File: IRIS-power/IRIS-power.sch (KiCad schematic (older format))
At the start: 11 parts, among them J11 Powerpole, J12 PJ-047AH, U11 TVS1400DRV, U12 TVS1400DRV

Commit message: Updated IRIS power board for V4
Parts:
- removed U11, U12: TVS1400DRV, star-common-lib:WSON-6-1EP_2x2mm_Hand_Solder, symbol star-common-lib:TVS1400DRV
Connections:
- wire segments 63 -> 61
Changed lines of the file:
@@
 Wire Wire Line
 	1300 3750 1900 3750
-Wire Wire Line
-	1900 2900 1300 2900
 Connection ~ 1300 2900
-Wire Wire Line
-	1300 2300 1900 2300
-$Comp
-L star-common-lib:TVS1400DRV U?
-U 1 1 5F2F2145
-P 1900 2600
-AR Path="/5F38FD4F/5F2F2145" Ref="U?"  Part="1"
-AR Path="/5F2F2145" Ref="U11"  Part="1"
-F 0 "U11" H 2029 2646 50  0000 L CNN
-F 1 "TVS1400DRV" H 2029 2555 50  0000 L CNN
-F 2 "star-common-lib:WSON-6-1EP_2x2mm_Hand_Solder" H 2100 2250 50  0001 C CNN
-F 3 "http://www.ti.com/lit/ds/symlink/tvs1400.pdf" H 1800 2600 50  0001 C CNN
-	1    1900 2600
-	1    0    0    -1
-$EndComp
-Connection ~ 1900 2300
-$Comp
-L star-common-lib:TVS1400DRV U?
-U 1 1 5F2F214D
-P 1900 4050
-AR Path="/5F38FD4F/5F2F214D" Ref="U?"  Part="1"
-AR Path="/5F2F214D" Ref="U12"  Part="1"
-F 0 "U12" H 2029 4096 50  0000 L CNN
-F 1 "TVS1400DRV" H 2029 4005 50  0000 L CNN
-F 2 "star-common-lib:WSON-6-1EP_2x2mm_Hand_Solder" H 2100 3700 50  0001 C CNN
-F 3 "http://www.ti.com/lit/ds/symlink/tvs1400.pdf" H 1800 4050 50  0001 C CNN
-	1    1900 4050
-	1    0    0    -1
-$EndComp
 Connection ~ 1900 3750
 Wire Wire Line
@@
 Wire Wire Line
 	1300 4350 1900 4350
-Connection ~ 1900 4350
 Wire Wire Line
 	1900 3750 3100 3750
-Wire Wire Line
-	1900 2300 2800 2300
 Wire Wire Line
 	2800 2300 2800 3550
 Connection ~ 2800 2300
 Wire Wire Line
-	1900 2900 2600 2900
-Wire Wire Line
 	2600 2900 2600 2500
 Wire Wire Line
 	2600 2500 7850 2500
-Connection ~ 1900 2900
 Wire Wire Line
 	9500 4650 9500 2400
@@
 	1    0    0    -1
 $EndComp
+Wire Wire Line
+	1300 2900 2600 2900
+Wire Wire Line
+	1300 2300 2800 2300
 $EndSCHEMATC

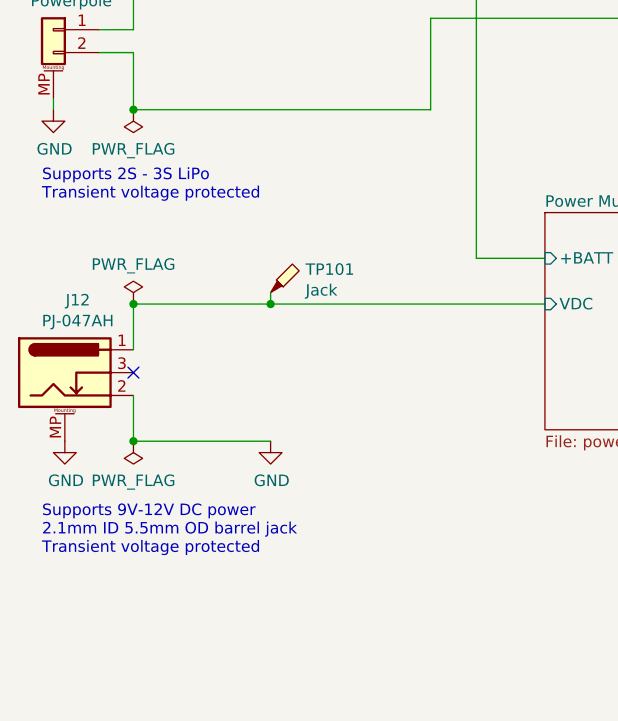
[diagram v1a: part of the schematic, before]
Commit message: Improved fuel gauge layout
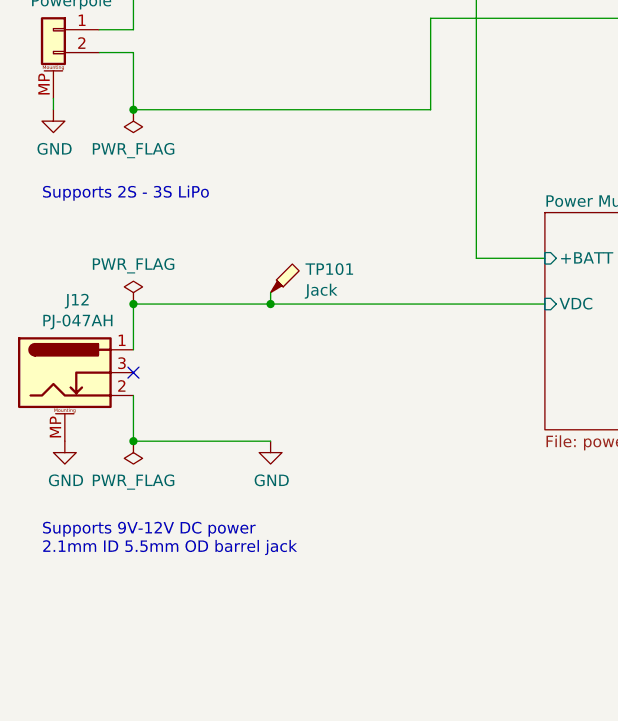
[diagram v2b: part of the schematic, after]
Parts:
- J11: Digikey PN (none) -> 2243-1336G1-ND
- J12: Digikey PN (none) -> CP-047AH-ND
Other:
- note added: "Supports 2S - 3S LiPo"
- note added: "Supports 9V-12V DC power\n2.1mm ID 5.5mm OD barrel jack"
- note removed: "Supports 2S - 3S LiPo\nTransient voltage protected"
- note removed: "Supports 9V-12V DC power\n2.1mm ID 5.5mm OD barrel jack\nTransient voltage protected"
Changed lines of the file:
@@
 	1300 2650 1300 2900
 Text Notes 900  3300 0    50   ~ 0
-Supports 2S - 3S LiPo\nTransient voltage protected
+Supports 2S - 3S LiPo
 $Comp
 L power:GND #PWR0101
@@
 F 2 "star-common-lib:CUI_PJ-047AH" H 1050 4010 50  0001 C CNN
 F 3 "~" H 1050 4010 50  0001 C CNN
+F 4 "CP-047AH-ND" H 1000 4050 50  0001 C CNN "Digikey PN"
 	1    1000 4050
 	1    0    0    -1
@@
 Wire Wire Line
 	1300 3950 1300 3750
-Text Notes 900  4850 0    50   ~ 0
-Supports 9V-12V DC power\n2.1mm ID 5.5mm OD barrel jack\nTransient voltage protected
 $Comp
 L power:PWR_FLAG #FLG?
@@
 F 2 "star-common-lib:Powerpole_1336G1" H 950 2550 50  0001 C CNN
 F 3 "~" H 950 2550 50  0001 C CNN
+F 4 "2243-1336G1-ND" H 950 2550 50  0001 C CNN "Digikey PN"
 	1    950  2550
 	-1   0    0    -1
@@
 Wire Wire Line
 	1300 2300 2800 2300
+Text Notes 900  4850 0    50   ~ 0
+Supports 9V-12V DC power\n2.1mm ID 5.5mm OD barrel jack
 $EndSCHEMATC

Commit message: Adjusted silkscreen
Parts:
- TP101, TP102, TP103, TP104, TP105, TP106, TP107: Digikey PN (none) -> 36-5006-ND
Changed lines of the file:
@@
 F 2 "TestPoint:TestPoint_Keystone_5000-5004_Miniature" H 4550 3500 50  0001 C CNN
 F 3 "~" H 4550 3500 50  0001 C CNN
+F 4 "36-5006-ND" H 4350 3500 50  0001 C CNN "Digikey PN"
 	1    4350 3500
 	1    0    0    -1
@@
 F 2 "TestPoint:TestPoint_Keystone_5000-5004_Miniature" H 4600 2250 50  0001 C CNN
 F 3 "~" H 4600 2250 50  0001 C CNN
+F 4 "36-5006-ND" H 4400 2250 50  0001 C CNN "Digikey PN"
 	1    4400 2250
 	1    0    0    -1
@@
 F 2 "TestPoint:TestPoint_Keystone_5000-5004_Miniature" H 6100 3500 50  0001 C CNN
 F 3 "~" H 6100 3500 50  0001 C CNN
+F 4 "36-5006-ND" H 5900 3500 50  0001 C CNN "Digikey PN"
 	1    5900 3500
 	1    0    0    -1
@@
 F 2 "TestPoint:TestPoint_Keystone_5000-5004_Miniature" H 7500 5000 50  0001 C CNN
 F 3 "~" H 7500 5000 50  0001 C CNN
+F 4 "36-5006-ND" H 7300 5000 50  0001 C CNN "Digikey PN"
 	1    7300 5000
 	1    0    0    -1
@@
 F 2 "TestPoint:TestPoint_Keystone_5000-5004_Miniature" H 7700 3550 50  0001 C CNN
 F 3 "~" H 7700 3550 50  0001 C CNN
+F 4 "36-5006-ND" H 7500 3550 50  0001 C CNN "Digikey PN"
 	1    7500 3550
 	1    0    0    -1
@@
 F 2 "TestPoint:TestPoint_Keystone_5000-5004_Miniature" H 9200 3500 50  0001 C CNN
 F 3 "~" H 9200 3500 50  0001 C CNN
+F 4 "36-5006-ND" H 9000 3500 50  0001 C CNN "Digikey PN"
 	1    9000 3500
 	1    0    0    -1
@@
 F 2 "TestPoint:TestPoint_Keystone_5000-5004_Miniature" H 2100 3700 50  0001 C CNN
 F 3 "~" H 2100 3700 50  0001 C CNN
+F 4 "36-5006-ND" H 1900 3700 50  0001 C CNN "Digikey PN"
 	1    1900 3700
 	1    0    0    -1

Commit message: USB C power prototype
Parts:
- removed J12: PJ-047AH, star-common-lib:CUI_PJ-047AH, symbol Connector:Barrel_Jack_Switch_MountingPin
- TP101: value Jack -> VBUS
- TP102: value Mux -> +5V
- TP104: value 5V -> Mux
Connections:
- net 5V Backup/+5V renamed 5V Backup/+MUX
- net 5V Supply/+MUX renamed 5V Supply/+5V
- net Fuel Gauge/+BATT renamed 5V Supply/+BATT
- net Power Mux/VDC renamed Power Mux/VUSB
- no-connect marks 1 -> 0
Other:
- note removed: "Supports 9V-12V DC power\n2.1mm ID 5.5mm OD barrel jack"
- moved on the sheet: TP102
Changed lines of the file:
@@
 $Descr A4 11693 8268
 encoding utf-8
-Sheet 1 8
+Sheet 1 9
 Title ""
 Date "2020-08-06"
@@
 $EndSheet
 $Sheet
-S 3100 3350 950  950
+S 3400 4650 950  950
 U 5F3CE42C
 F0 "Power Mux" 50
 F1 "power_mux.sch" 50
-F2 "VDC" I L 3100 3750 50
-F3 "+MUX" O R 4050 3550 50
-F4 "+BATT" I L 3100 3550 50
+F2 "+MUX" O R 4350 4850 50
+F3 "+5V" I L 3400 4850 50
+F4 "VUSB" I L 3400 5050 50
 $EndSheet
 $Sheet
@@
 $EndSheet
 $Sheet
-S 4650 3350 950  950
+S 1050 3800 950  950
 U 5F41B5C3
 F0 "5V Supply" 50
 F1 "5V_supply.sch" 50
-F2 "+MUX" I L 4650 3550 50
-F3 "+5V" O R 5600 3550 50
+F2 "+BATT" I L 1050 4000 50
+F3 "+5V" O R 2000 4000 50
 $EndSheet
 $Sheet
@@
 F0 "5V Backup" 50
 F1 "5V_backup.sch" 50
-F2 "+5V" I L 6200 3550 50
+F2 "+MUX" I L 6200 3550 50
 F3 "VSYS" O R 7150 3550 50
 F4 "SDA" B R 7150 3950 50
@@
 $EndSheet
 Wire Wire Line
-	2800 3550 3100 3550
-Wire Wire Line
-	4050 3550 4350 3550
-Wire Wire Line
-	4650 4850 4350 4850
-Wire Wire Line
-	4350 4850 4350 3550
-Connection ~ 4350 3550
-Wire Wire Line
-	4350 3550 4650 3550
+	4650 4850 4500 4850
 Wire Wire Line
 	8800 3550 9000 3550
@@
 Text Notes 900  3300 0    50   ~ 0
 Supports 2S - 3S LiPo
-$Comp
-L power:GND #PWR0101
-U 1 1 5F2F2116
-P 1000 4350
-AR Path="/5F2F2116" Ref="#PWR0101"  Part="1"
-AR Path="/5F38FD4F/5F2F2116" Ref="#PWR?"  Part="1"
-F 0 "#PWR0101" H 1000 4100 50  0001 C CNN
-F 1 "GND" H 1005 4177 50  0000 C CNN
-F 2 "" H 1000 4350 50  0001 C CNN
-F 3 "" H 1000 4350 50  0001 C CNN
-	1    1000 4350
-	1    0    0    -1
-$EndComp
-$Comp
-L power:GND #PWR0102
-U 1 1 5F2F211C
-P 1900 4350
-AR Path="/5F2F211C" Ref="#PWR0102"  Part="1"
-AR Path="/5F38FD4F/5F2F211C" Ref="#PWR?"  Part="1"
-F 0 "#PWR0102" H 1900 4100 50  0001 C CNN
-F 1 "GND" H 1905 4177 50  0000 C CNN
-F 2 "" H 1900 4350 50  0001 C CNN
-F 3 "" H 1900 4350 50  0001 C CNN
-	1    1900 4350
-	1    0    0    -1
-$EndComp
-$Comp
-L Connector:Barrel_Jack_Switch_MountingPin J12
-U 1 1 5F2F2122
-P 1000 4050
-AR Path="/5F2F2122" Ref="J12"  Part="1"
-AR Path="/5F38FD4F/5F2F2122" Ref="J?"  Part="1"
-F 0 "J12" H 1057 4367 50  0000 C CNN
-F 1 "PJ-047AH" H 1057 4276 50  0000 C CNN
-F 2 "star-common-lib:CUI_PJ-047AH" H 1050 4010 50  0001 C CNN
-F 3 "~" H 1050 4010 50  0001 C CNN
-F 4 "CP-047AH-ND" H 1000 4050 50  0001 C CNN "Digikey PN"
-	1    1000 4050
-	1    0    0    -1
-$EndComp
-NoConn ~ 1300 4050
-Wire Wire Line
-	1300 3950 1300 3750
 $Comp
 L power:PWR_FLAG #FLG?
@@
 $EndComp
 Connection ~ 1300 2300
-$Comp
-L power:PWR_FLAG #FLG?
-U 1 1 5F2F2134
-P 1300 3750
-AR Path="/5F38FD4F/5F2F2134" Ref="#FLG?"  Part="1"
-AR Path="/5F2F2134" Ref="#FLG0103"  Part="1"
-F 0 "#FLG0103" H 1300 3825 50  0001 C CNN
-F 1 "PWR_FLAG" H 1300 3923 50  0000 C CNN
-F 2 "" H 1300 3750 50  0001 C CNN
-F 3 "~" H 1300 3750 50  0001 C CNN
-	1    1300 3750
-	1    0    0    -1
-$EndComp
-Connection ~ 1300 3750
 $Comp
 L power:PWR_FLAG #FLG?
@@
 	-1   0    0    1
 $EndComp
-Wire Wire Line
-	1300 3750 1900 3750
 Connection ~ 1300 2900
-Connection ~ 1900 3750
-Wire Wire Line
-	1300 4150 1300 4350
-Wire Wire Line
-	1300 4350 1900 4350
-Wire Wire Line
-	1900 3750 3100 3750
-Wire Wire Line
-	2800 2300 2800 3550
-Connection ~ 2800 2300
 Wire Wire Line
 	2600 2900 2600 2500
@@
 	7200 4050 7200 4750
 $Comp
-L power:PWR_FLAG #FLG?
-U 1 1 5F359A7E
-P 1300 4350
-AR Path="/5F38FD4F/5F359A7E" Ref="#FLG?"  Part="1"
-AR Path="/5F359A7E" Ref="#FLG0104"  Part="1"
-F 0 "#FLG0104" H 1300 4425 50  0001 C CNN
-F 1 "PWR_FLAG" H 1300 4523 50  0000 C CNN
-F 2 "" H 1300 4350 50  0001 C CNN
-F 3 "~" H 1300 4350 50  0001 C CNN
-	1    1300 4350
-	-1   0    0    1
-$EndComp
-Connection ~ 1300 4350
-$Comp
 L Connector:TestPoint_Probe TP102
 U 1 1 5F31D262
-P 4350 3500
-F 0 "TP102" H 4503 3601 50  0000 L CNN
-F 1 "Mux" H 4503 3510 50  0000 L CNN
-F 2 "TestPoint:TestPoint_Keystone_5000-5004_Miniature" H 4550 3500 50  0001 C CNN
-F 3 "~" H 4550 3500 50  0001 C CNN
-F 4 "36-5006-ND" H 4350 3500 50  0001 C CNN "Digikey PN"
-	1    4350 3500
+P 2600 4000
+F 0 "TP102" H 2753 4101 50  0000 L CNN
+F 1 "+5V" H 2753 4010 50  0000 L CNN
+F 2 "TestPoint:TestPoint_Keystone_5000-5004_Miniature" H 2800 4000 50  0001 C CNN
+F 3 "~" H 2800 4000 50  0001 C CNN
+F 4 "36-5006-ND" H 2600 4000 50  0001 C CNN "Digikey PN"
+	1    2600 4000
 	1    0    0    -1
 $EndComp
@@
 P 5900 3500
 F 0 "TP104" H 6053 3601 50  0000 L CNN
-F 1 "5V" H 6053 3510 50  0000 L CNN
+F 1 "Mux" H 6053 3510 50  0000 L CNN
 F 2 "TestPoint:TestPoint_Keystone_5000-5004_Miniature" H 6100 3500 50  0001 C CNN
 F 3 "~" H 6100 3500 50  0001 C CNN
@@
 	1    0    0    -1
 $EndComp
-$Comp
-L Connector:TestPoint_Probe TP101
-U 1 1 5F320DDB
-P 1900 3700
-F 0 "TP101" H 2053 3801 50  0000 L CNN
-F 1 "Jack" H 2053 3710 50  0000 L CNN
-F 2 "TestPoint:TestPoint_Keystone_5000-5004_Miniature" H 2100 3700 50  0001 C CNN
-F 3 "~" H 2100 3700 50  0001 C CNN
-F 4 "36-5006-ND" H 1900 3700 50  0001 C CNN "Digikey PN"
-	1    1900 3700
-	1    0    0    -1
-$EndComp
-Wire Wire Line
-	5600 3550 5900 3550
 Wire Wire Line
 	5900 3550 5900 3500
@@
 	5900 3550 6200 3550
 Wire Wire Line
-	4350 3550 4350 3500
-Wire Wire Line
-	2800 2300 4400 2300
-Wire Wire Line
 	4400 2300 4400 2250
 Connection ~ 4400 2300
@@
 Wire Wire Line
 	7300 5050 9700 5050
-Wire Wire Line
-	1900 3750 1900 3700
 Wire Wire Line
 	7600 3650 7600 2700
@@
 Wire Wire Line
 	1300 2900 2600 2900
-Wire Wire Line
-	1300 2300 2800 2300
-Text Notes 900  4850 0    50   ~ 0
-Supports 9V-12V DC power\n2.1mm ID 5.5mm OD barrel jack
+$Sheet
+S 1050 5150 950  950
+U 5FB7ED68
+F0 "USB Connector" 50
+F1 "USB_Conn.sch" 50
+F2 "VUSB" O R 2000 5550 50
+$EndSheet
+Wire Wire Line
+	1300 2300 2200 2300
+Wire Wire Line
+	4500 4850 4500 3550
+Wire Wire Line
+	4500 3550 5900 3550
+Connection ~ 4500 4850
+Wire Wire Line
+	4500 4850 4350 4850
+Wire Wire Line
+	2000 4000 2600 4000
+Wire Wire Line
+	2600 4000 2600 4850
+Wire Wire Line
+	2600 4850 3400 4850
+Connection ~ 2600 4000
+Wire Wire Line
+	1050 4000 800  4000
+Wire Wire Line
+	800  4000 800  3500
+Wire Wire Line
+	800  3500 2200 3500
+Wire Wire Line
+	2200 3500 2200 2300
+Connection ~ 2200 2300
+Wire Wire Line
+	2200 2300 4400 2300
+Wire Wire Line
+	2600 5550 2600 5050
+Wire Wire Line
+	2600 5050 3400 5050
+Wire Wire Line
+	2000 5550 2600 5550
+$Comp
+L Connector:TestPoint_Probe TP101
+U 1 1 5FC19CF4
+P 2600 5550
+F 0 "TP101" H 2753 5651 50  0000 L CNN
+F 1 "VBUS" H 2753 5560 50  0000 L CNN
+F 2 "TestPoint:TestPoint_Keystone_5000-5004_Miniature" H 2800 5550 50  0001 C CNN
+F 3 "~" H 2800 5550 50  0001 C CNN
+F 4 "36-5006-ND" H 2600 5550 50  0001 C CNN "Digikey PN"
+	1    2600 5550
+	1    0    0    -1
+$EndComp
 $EndSCHEMATC

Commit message: Updated to V4.01
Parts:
- removed TP101: VBUS, TestPoint:TestPoint_Keystone_5000-5004_Miniature, symbol Connector:TestPoint_Probe
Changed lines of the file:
@@
 Wire Wire Line
 	2000 5550 2600 5550
-$Comp
-L Connector:TestPoint_Probe TP101
-U 1 1 5FC19CF4
-P 2600 5550
-F 0 "TP101" H 2753 5651 50  0000 L CNN
-F 1 "VBUS" H 2753 5560 50  0000 L CNN
-F 2 "TestPoint:TestPoint_Keystone_5000-5004_Miniature" H 2800 5550 50  0001 C CNN
-F 3 "~" H 2800 5550 50  0001 C CNN
-F 4 "36-5006-ND" H 2600 5550 50  0001 C CNN "Digikey PN"
-	1    2600 5550
-	1    0    0    -1
-$EndComp
 $EndSCHEMATC

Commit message: IRIS V4.02
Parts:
- added FID1, FID2, FID3: Fiducial, Fiducial:Fiducial_1.5mm_Mask3mm, symbol Mechanical:Fiducial
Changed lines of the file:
@@
 Wire Wire Line
 	2000 5550 2600 5550
+$Comp
+L Mechanical:Fiducial FID2
+U 1 1 5FD5D545
+P 2200 2150
+F 0 "FID2" H 2285 2196 50  0000 L CNN
+F 1 "Fiducial" H 2285 2105 50  0000 L CNN
+F 2 "Fiducial:Fiducial_1.5mm_Mask3mm" H 2200 2150 50  0001 C CNN
+F 3 "~" H 2200 2150 50  0001 C CNN
+	1    2200 2150
+	1    0    0    -1
+$EndComp
+$Comp
+L Mechanical:Fiducial FID1
+U 1 1 5FD5DDFA
+P 2200 1950
+F 0 "FID1" H 2285 1996 50  0000 L CNN
+F 1 "Fiducial" H 2285 1905 50  0000 L CNN
+F 2 "Fiducial:Fiducial_1.5mm_Mask3mm" H 2200 1950 50  0001 C CNN
+F 3 "~" H 2200 1950 50  0001 C CNN
+	1    2200 1950
+	1    0    0    -1
+$EndComp
+$Comp
+L Mechanical:Fiducial FID3
+U 1 1 5FD618C3
+P 2200 1750
+F 0 "FID3" H 2285 1796 50  0000 L CNN
+F 1 "Fiducial" H 2285 1705 50  0000 L CNN
+F 2 "Fiducial:Fiducial_1.5mm_Mask3mm" H 2200 1750 50  0001 C CNN
+F 3 "~" H 2200 1750 50  0001 C CNN
+	1    2200 1750
+	1    0    0    -1
+$EndComp
 $EndSCHEMATC
